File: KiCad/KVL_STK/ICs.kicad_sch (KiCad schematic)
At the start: 48 parts, among them J1 AudioJack2_Ground, J2 Conn_01x04, J3 AudioJack2_Ground, J4 Conn_01x08, U1 74HC164, U2 74HC165, U3 74HC165, U5 ADAU1761BCPZ, U6 MIC2005A-1YM5-TR

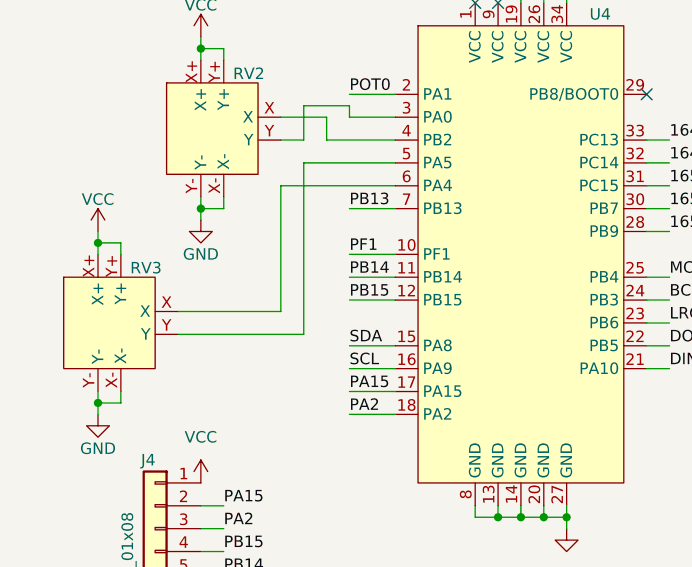
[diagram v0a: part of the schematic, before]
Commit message: Added 30 RGB LEDs.
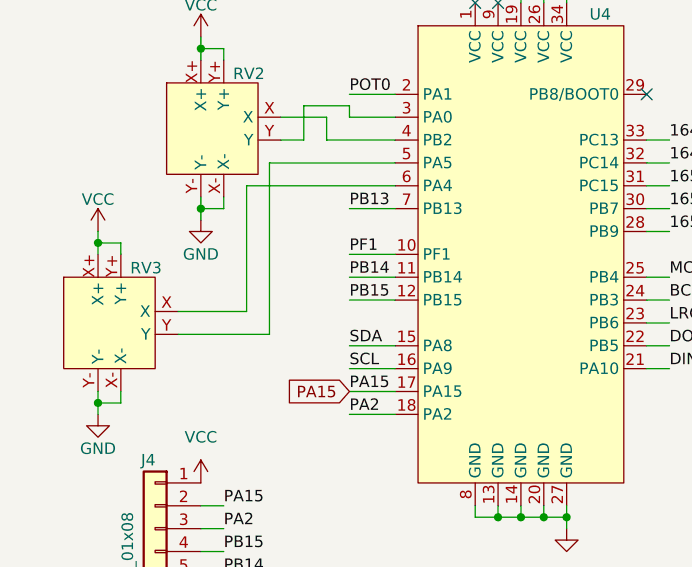
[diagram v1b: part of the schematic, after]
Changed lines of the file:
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@@
 	(wire
 		(pts
-			(xy 45.72 72.39) (xy 31.75 72.39)
+			(xy 41.91 72.39) (xy 31.75 72.39)
 		)
 		(stroke
@@
 	(wire
 		(pts
-			(xy 45.72 53.34) (xy 45.72 72.39)
+			(xy 41.91 53.34) (xy 41.91 72.39)
 		)
 		(stroke
@@
 	(wire
 		(pts
-			(xy 43.18 69.85) (xy 43.18 55.88)
+			(xy 39.37 69.85) (xy 39.37 55.88)
 		)
 		(stroke
@@
 	(wire
 		(pts
-			(xy 43.18 69.85) (xy 31.75 69.85)
+			(xy 39.37 69.85) (xy 31.75 69.85)
 		)
 		(stroke
@@
 	(wire
 		(pts
-			(xy 43.18 55.88) (xy 55.88 55.88)
+			(xy 39.37 55.88) (xy 55.88 55.88)
 		)
 		(stroke
@@
 	(wire
 		(pts
-			(xy 45.72 53.34) (xy 55.88 53.34)
+			(xy 41.91 53.34) (xy 55.88 53.34)
 		)
 		(stroke
@@
 			(effects
 				(font
+					(size 1.27 1.27)
+				)
+				(justify right)
+				(hide yes)
+			)
+		)
+	)
+	(global_label "PA15"
+		(shape input)
+		(at 50.8 78.74 180)
+		(fields_autoplaced yes)
+		(effects
+			(font
+				(size 1.27 1.27)
+			)
+			(justify right)
+		)
+		(property "Intersheetrefs" "${INTERSHEET_REFS}"
+			(at 43.0372 78.74 0)
+			(effects
+				(font
